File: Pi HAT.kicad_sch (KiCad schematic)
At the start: 11 parts, among them J1 Screw_Terminal_01x04, J4 Barrel_Jack, J5 Screw_Terminal_01x03, J6 Screw_Terminal_01x03, J7 GPIO_CONNECTOR, Q1 S8550

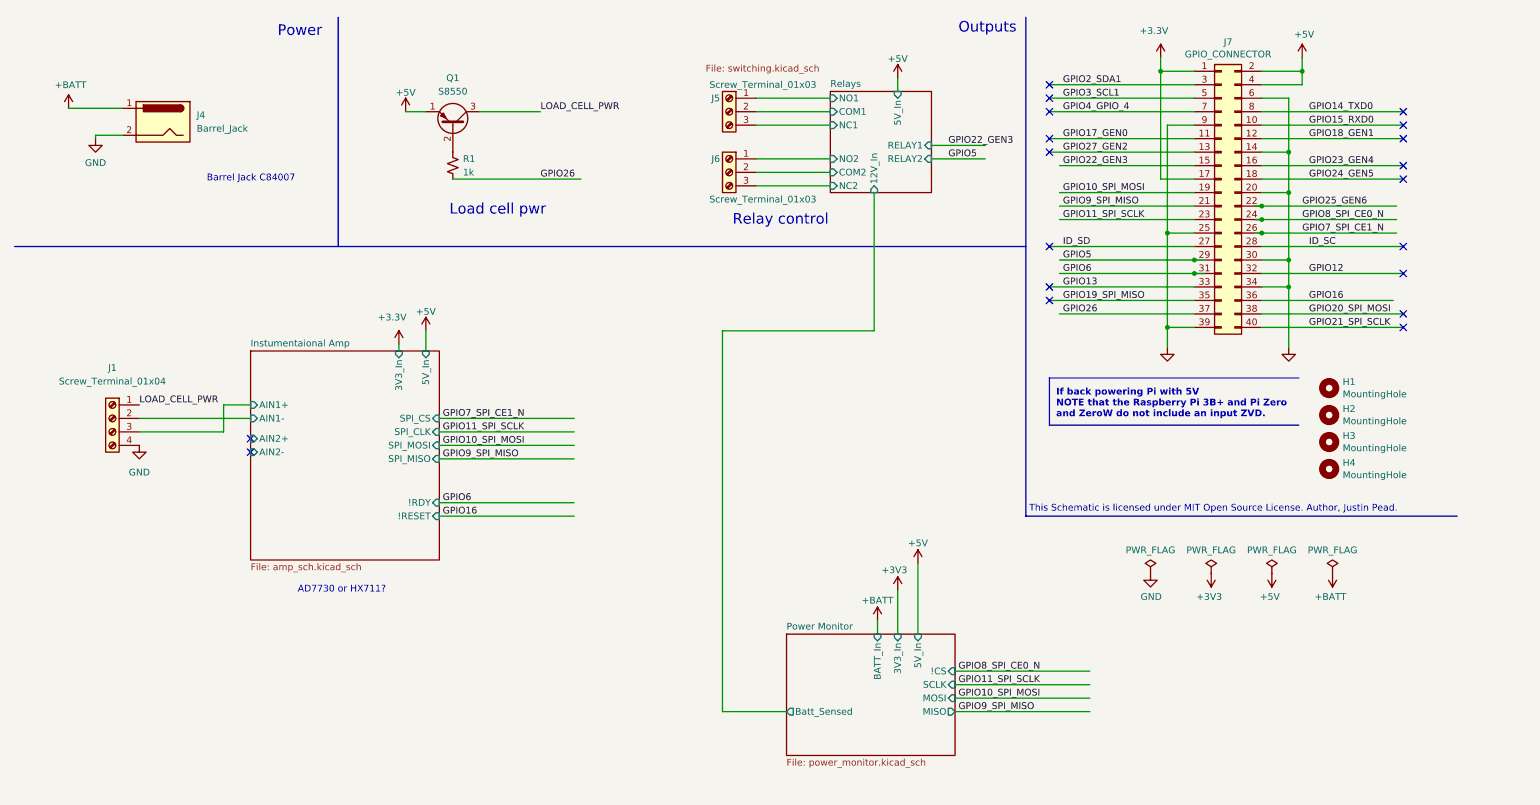
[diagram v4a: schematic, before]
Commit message: Changes made to the AD7730 circuit. HX711 circuit added and AD7730 sidestepped.
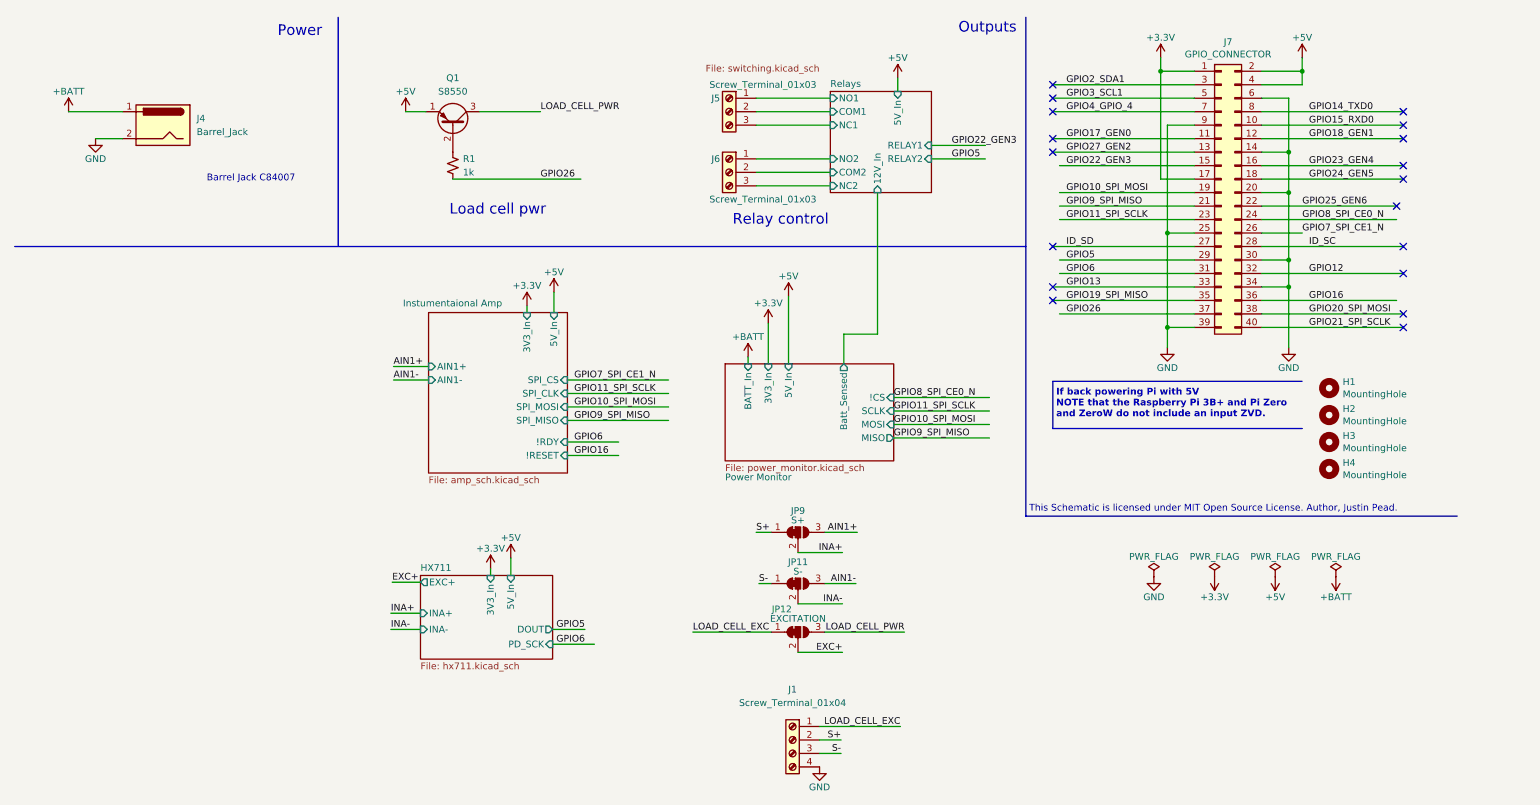
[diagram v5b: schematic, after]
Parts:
- added JP11: S-, symbol Jumper:SolderJumper_3_Bridged12
- added JP12: EXCITATION, symbol Jumper:SolderJumper_3_Bridged12
- added JP9: S+, symbol Jumper:SolderJumper_3_Bridged12
- J5, J6: Populate 0 -> 1
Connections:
- net LOAD_CELL_PWR: now also JP12.3 (B); no longer J1.1 (Pin_1)
- net +3V3 renamed +3.3V
- net Instumentaional Amp/AIN1+ renamed S-
- net S-: now also JP11.1 (A)
- net Instumentaional Amp/AIN1- renamed S+
- net S+: now also JP9.1 (A)
- new net AIN1+: JP9.3 (B)
- new net AIN1-: JP11.3 (B)
- new net EXC+: JP12.2 (C)
- new net INA+: JP9.2 (C)
- new net INA-: JP11.2 (C)
- new net LOAD_CELL_EXC: J1.1 (Pin_1), JP12.1 (A)
- no-connect marks 19 -> 18
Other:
- added sheet HX711 (hx711.kicad_sch)
- sheet Instumentaional Amp ports: added none; removed AIN2+, AIN2-
- note removed: "AD7730 or HX711?"
- moved on the sheet: J1, J4

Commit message: Added footprints for HX711 circuit on PCB and modified pin assignment
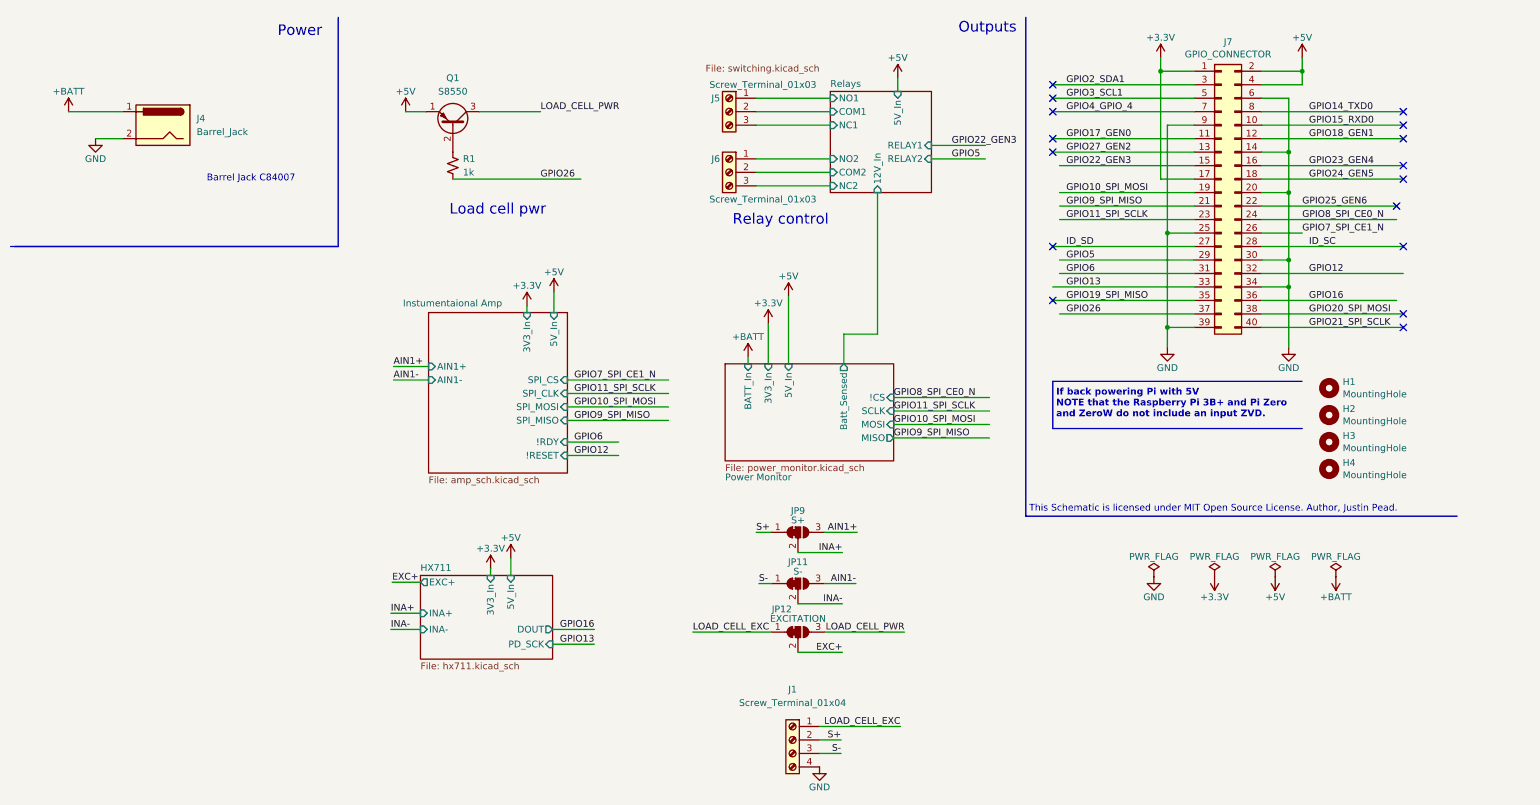
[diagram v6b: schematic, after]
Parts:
- JP11, JP12, JP9: footprint (none) -> Jumper:SolderJumper-3_P1.3mm_Bridged2Bar12_RoundedPad1.0x1.5mm
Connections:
- no-connect marks 18 -> 16
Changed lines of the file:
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@@
   (no_connect (at 208.28 38.1))
   (no_connect (at 274.32 33.02))
-  (no_connect (at 274.32 60.96))
   (no_connect (at 208.28 35.56))
   (no_connect (at 208.28 25.4))
   (no_connect (at 274.32 68.58))
-  (no_connect (at 208.28 63.5))
   (no_connect (at 274.32 55.88))
   (no_connect (at 208.28 66.04))
@@
     (stroke (width 0) (type default))
   )
-  (polyline (pts (xy 73.66 55.88) (xy 203.2 55.88))
+  (polyline (pts (xy 73.66 55.88) (xy 11.938 55.88))
     (stroke (width 0) (type default))
   )
@@
     (stroke (width 0) (type default))
   )
-  (wire (pts (xy 114.046 128.016) (xy 120.142 128.016))
+  (wire (pts (xy 114.046 128.016) (xy 121.92 128.016))
     (stroke (width 0) (type default))
   )
@@
     (effects (font (size 1.27 1.27)) (justify left bottom))
   )
-  (label "GPIO5" (at 120.142 128.016 180) (fields_autoplaced)
-    (effects (font (size 1.27 1.27)) (justify right bottom))
-  )
-  (label "GPIO16" (at 118.11 95.25 0) (fields_autoplaced)
+  (label "GPIO12" (at 118.11 95.25 0) (fields_autoplaced)
     (effects (font (size 1.27 1.27)) (justify left bottom))
   )
@@
     (effects (font (size 1.27 1.27)) (justify left bottom))
   )
+  (label "GPIO13" (at 121.92 130.81 180) (fields_autoplaced)
+    (effects (font (size 1.27 1.27)) (justify right bottom))
+  )
   (label "GPIO19_SPI_MISO" (at 210.82 66.04 0) (fields_autoplaced)
     (effects (font (size 1.27 1.27)) (justify left bottom))
@@
     (effects (font (size 1.27 1.27)) (justify right bottom))
   )
+  (label "GPIO16" (at 121.92 128.016 180) (fields_autoplaced)
+    (effects (font (size 1.27 1.27)) (justify right bottom))
+  )
   (label "GPIO5" (at 189.23 39.37 0) (fields_autoplaced)
     (effects (font (size 1.27 1.27)) (justify left bottom))
@@
   )
   (label "LOAD_CELL_PWR" (at 180.34 128.524 180) (fields_autoplaced)
-    (effects (font (size 1.27 1.27)) (justify right bottom))
-  )
-  (label "GPIO6" (at 120.142 130.81 180) (fields_autoplaced)
     (effects (font (size 1.27 1.27)) (justify right bottom))
   )
@@
       (effects (font (size 1.27 1.27)))
     )
-    (property "Footprint" "" (at 160.274 119.38 0)
+    (property "Footprint" "Jumper:SolderJumper-3_P1.3mm_Bridged2Bar12_RoundedPad1.0x1.5mm" (at 160.274 119.38 0)
       (effects (font (size 1.27 1.27)) hide)
     )
@@
       (effects (font (size 1.27 1.27)))
     )
-    (property "Footprint" "" (at 160.274 128.524 0)
+    (property "Footprint" "Jumper:SolderJumper-3_P1.3mm_Bridged2Bar12_RoundedPad1.0x1.5mm" (at 160.274 128.524 0)
       (effects (font (size 1.27 1.27)) hide)
     )
@@
       (effects (font (size 1.27 1.27)))
     )
-    (property "Footprint" "" (at 160.274 109.728 0)
-      (effects (font (size 1.27 1.27)) hide)
-    )
+    (property "Footprint" "Jumper:SolderJumper-3_P1.3mm_Bridged2Bar12_RoundedPad1.0x1.5mm" (at 160.274 109.728 0)
+      (effects (font (size 1.27 1.27)) hide)
+    )

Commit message: Fixed clearance violations and via sizing violations on pcb. Omitted 'mask aperture bridges' errors for jumpers.
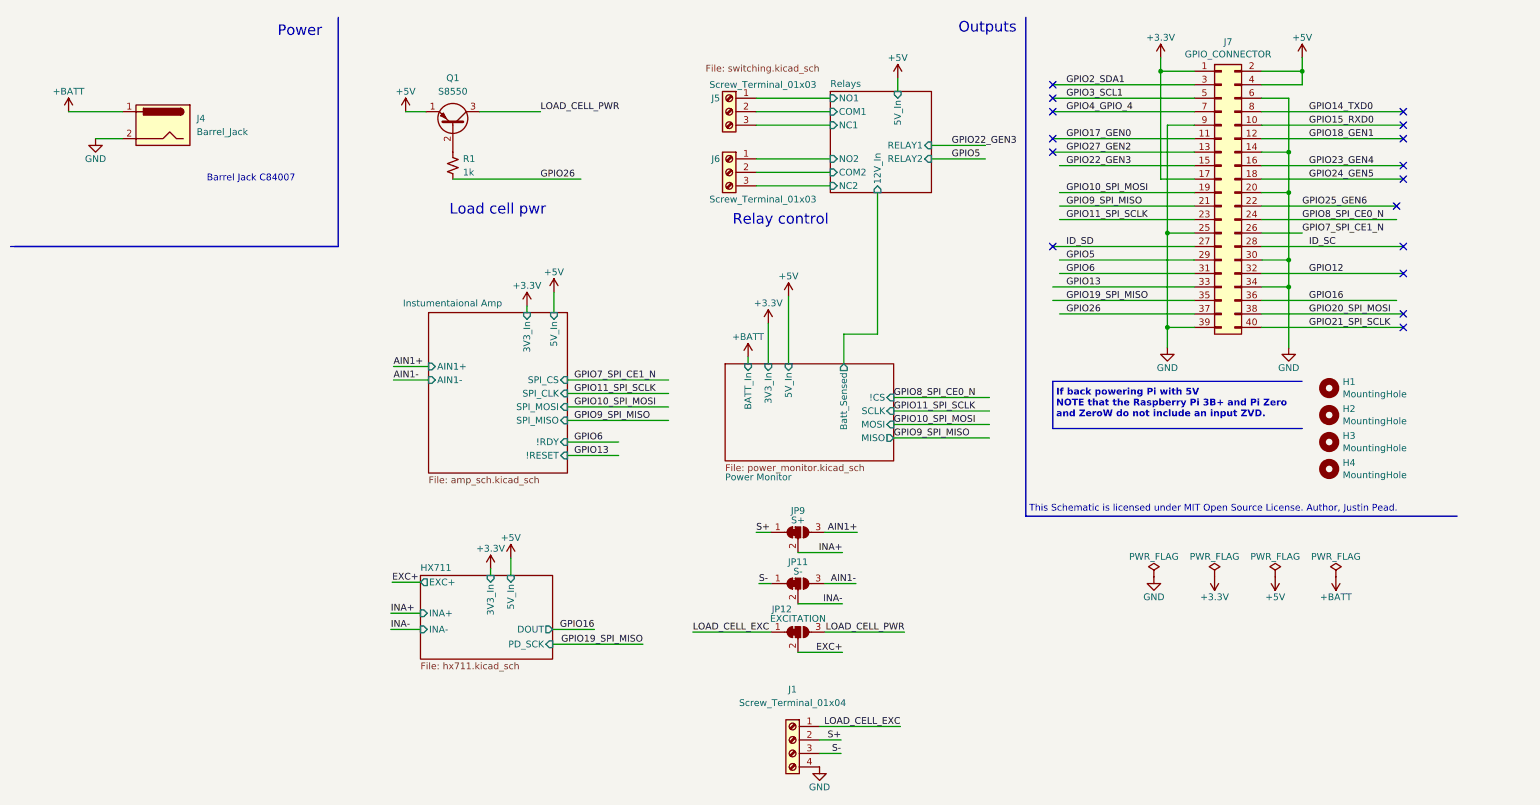
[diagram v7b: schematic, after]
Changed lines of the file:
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@@
   (no_connect (at 208.28 38.1))
   (no_connect (at 274.32 33.02))
+  (no_connect (at 274.32 60.96))
   (no_connect (at 208.28 35.56))
   (no_connect (at 208.28 25.4))
   (no_connect (at 274.32 68.58))
   (no_connect (at 274.32 55.88))
-  (no_connect (at 208.28 66.04))
   (wire (pts (xy 152.4 27.94) (xy 166.37 27.94))
     (stroke (width 0) (type default))
@@
     (stroke (width 0) (type default))
   )
-  (wire (pts (xy 114.046 130.81) (xy 121.92 130.81))
+  (wire (pts (xy 114.046 130.81) (xy 131.064 130.81))
     (stroke (width 0) (type default))
   )
@@
     (effects (font (size 1.27 1.27)) (justify left bottom))
   )
-  (label "GPIO12" (at 118.11 95.25 0) (fields_autoplaced)
+  (label "GPIO13" (at 118.11 95.25 0) (fields_autoplaced)
     (effects (font (size 1.27 1.27)) (justify left bottom))
   )
@@
     (effects (font (size 1.27 1.27)) (justify left bottom))
   )
-  (label "GPIO13" (at 121.92 130.81 180) (fields_autoplaced)
+  (label "GPIO19_SPI_MISO" (at 131.064 130.81 180) (fields_autoplaced)
     (effects (font (size 1.27 1.27)) (justify right bottom))
   )

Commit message: Added ground pour and fixed connections
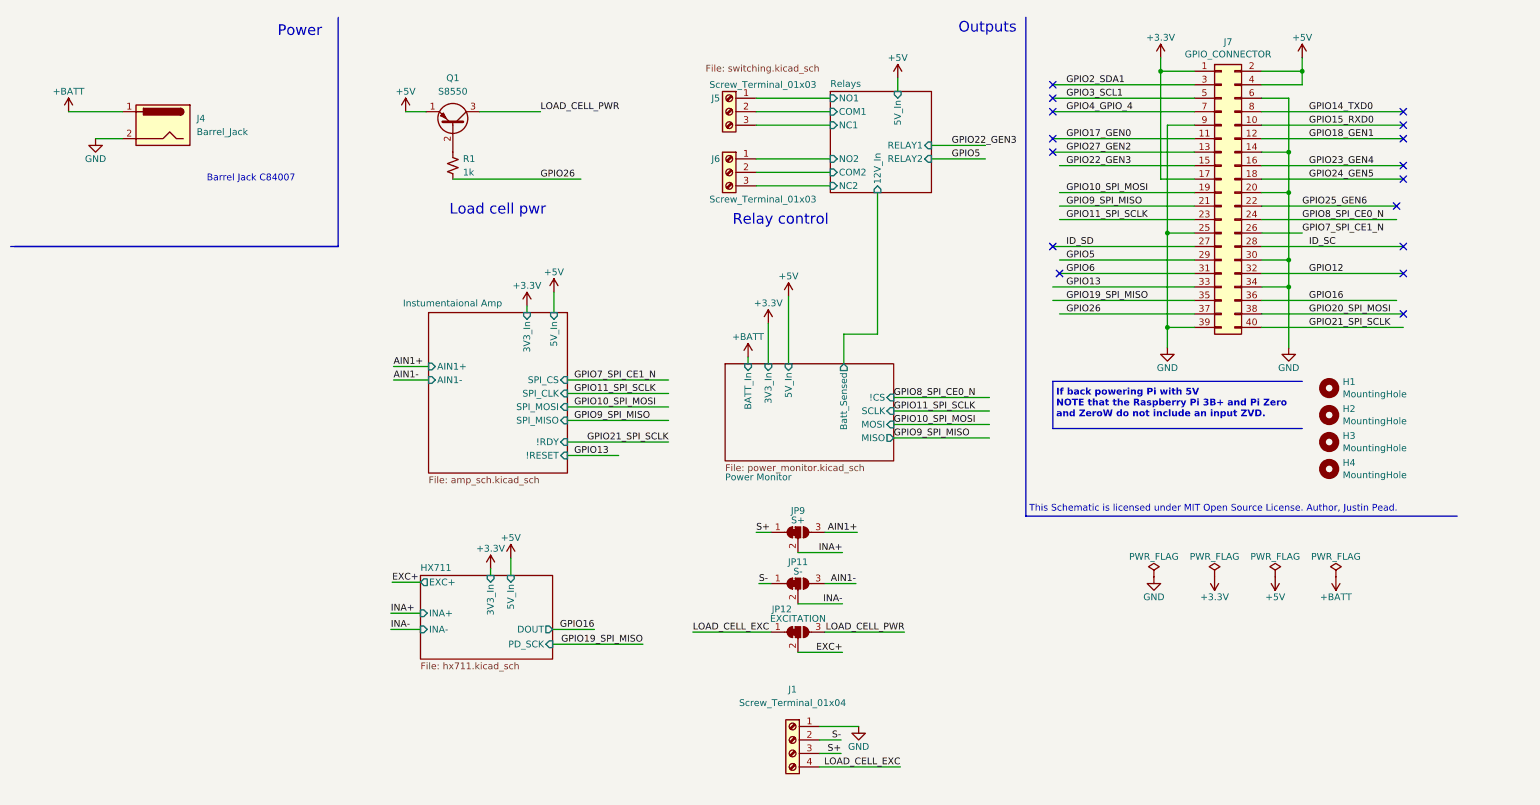
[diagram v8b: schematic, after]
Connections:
- net GND: now also J1.1 (Pin_1); no longer J1.4 (Pin_4)
- net LOAD_CELL_EXC: now also J1.4 (Pin_4); no longer J1.1 (Pin_1)
- net S+: now also J1.3 (Pin_3); no longer J1.2 (Pin_2)
- net S-: now also J1.2 (Pin_2); no longer J1.3 (Pin_3)
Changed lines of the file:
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@@
   )
   (no_connect (at 274.32 30.48))
-  (no_connect (at 274.32 71.12))
   (no_connect (at 208.28 30.48))
   (no_connect (at 274.32 35.56))
   (no_connect (at 274.32 43.18))
   (no_connect (at 208.28 27.94))
+  (no_connect (at 209.55 60.96))
   (no_connect (at 273.05 48.26))
   (no_connect (at 274.32 40.64))
@@
     (stroke (width 0) (type default))
   )
-  (wire (pts (xy 116.84 92.71) (xy 126.492 92.71))
+  (wire (pts (xy 116.84 92.71) (xy 135.89 92.71))
     (stroke (width 0) (type default))
   )
@@
     (stroke (width 0) (type default))
   )
+  (wire (pts (xy 164.338 146.304) (xy 171.704 146.304))
+    (stroke (width 0) (type default))
+  )
   (wire (pts (xy 160.274 123.19) (xy 168.656 123.19))
     (stroke (width 0) (type default))
@@
     (stroke (width 0) (type default))
   )
-  (wire (pts (xy 164.338 146.304) (xy 179.578 146.304))
-    (stroke (width 0) (type default))
-  )
   (polyline (pts (xy 73.66 55.88) (xy 11.938 55.88))
     (stroke (width 0) (type default))
@@
   )
   (wire (pts (xy 209.55 48.26) (xy 234.95 48.26))
+    (stroke (width 0) (type default))
+  )
+  (wire (pts (xy 164.338 153.924) (xy 179.578 153.924))
     (stroke (width 0) (type default))
   )
@@
     (effects (font (size 1.27 1.27)) (justify left bottom))
   )
-  (label "S-" (at 168.402 151.384 180) (fields_autoplaced)
+  (label "S+" (at 168.402 151.384 180) (fields_autoplaced)
     (effects (font (size 1.27 1.27)) (justify right bottom))
   )
@@
     (effects (font (size 1.27 1.27)) (justify left bottom))
   )
+  (label "LOAD_CELL_EXC" (at 179.578 153.924 180) (fields_autoplaced)
+    (effects (font (size 1.27 1.27)) (justify right bottom))
+  )
   (label "GPIO2_SDA1" (at 210.82 25.4 0) (fields_autoplaced)
     (effects (font (size 1.27 1.27)) (justify left bottom))
@@
     (effects (font (size 1.27 1.27)) (justify left bottom))
   )
-  (label "LOAD_CELL_EXC" (at 179.578 146.304 180) (fields_autoplaced)
-    (effects (font (size 1.27 1.27)) (justify right bottom))
-  )
   (label "GPIO8_SPI_CE0_N" (at 178.308 84.328 0) (fields_autoplaced)
     (effects (font (size 1.27 1.27)) (justify left bottom))
@@
     (effects (font (size 1.27 1.27)) (justify left bottom))
   )
-  (label "GPIO6" (at 118.11 92.71 0) (fields_autoplaced)
-    (effects (font (size 1.27 1.27)) (justify left bottom))
-  )
   (label "INA-" (at 83.566 128.016 0) (fields_autoplaced)
     (effects (font (size 1.27 1.27)) (justify left bottom))
@@
     (effects (font (size 1.27 1.27)) (justify left bottom))
   )
+  (label "GPIO21_SPI_SCLK" (at 135.89 92.71 180) (fields_autoplaced)
+    (effects (font (size 1.27 1.27)) (justify right bottom))
+  )
   (label "GPIO24_GEN5" (at 256.54 43.18 0) (fields_autoplaced)
     (effects (font (size 1.27 1.27)) (justify left bottom))
   )
-  (label "S+" (at 168.402 148.844 180) (fields_autoplaced)
+  (label "S-" (at 168.402 148.844 180) (fields_autoplaced)
     (effects (font (size 1.27 1.27)) (justify right bottom))
   )
@@
     )
   )
-  (symbol (lib_id "power:GND") (at 164.338 153.924 0) (unit 1)
-    (in_bom yes) (on_board yes) (dnp no)
-    (property "Reference" "#PWR048" (at 164.338 160.274 0)
-      (effects (font (size 1.27 1.27)) hide)
-    )
-    (property "Value" "GND" (at 164.338 157.734 0)
+  (symbol (lib_id "power:GND") (at 171.704 146.304 0) (unit 1)
+    (in_bom yes) (on_board yes) (dnp no)
+    (property "Reference" "#PWR048" (at 171.704 152.654 0)
+      (effects (font (size 1.27 1.27)) hide)
+    )
+    (property "Value" "GND" (at 171.704 150.114 0)
       (effects (font (size 1.27 1.27)))
     )
-    (property "Footprint" "" (at 164.338 153.924 0)
-      (effects (font (size 1.27 1.27)) hide)
-    )
-    (property "Datasheet" "" (at 164.338 153.924 0)
-      (effects (font (size 1.27 1.27)) hide)
-    )
+    (property "Footprint" "" (at 171.704 146.304 0)
+      (effects (font (size 1.27 1.27)) hide)
+    )
+    (property "Datasheet" "" (at 171.704 146.304 0)
+      (effects (font (size 1.27 1.27)) hide)
+    )
